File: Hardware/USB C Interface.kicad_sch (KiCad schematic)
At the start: 5 parts, among them J2 USB_C_Receptacle_USB2.0, U14 TPD4E02B04DQA

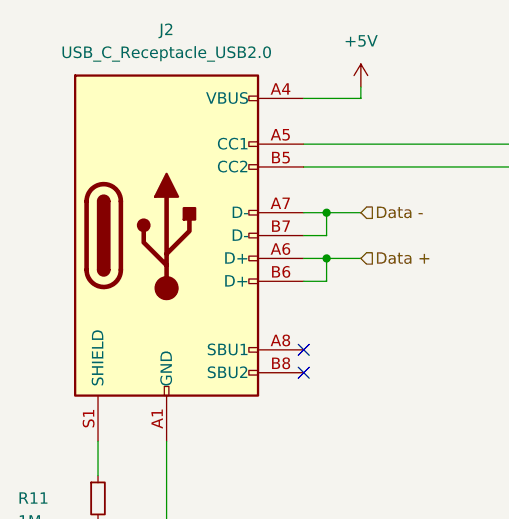
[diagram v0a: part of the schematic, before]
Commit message: Fix Reroute
Traces are getting messy, Moved the TOF sensors to be 3mm from edge of board. USB-C getting moved possibly. Changed Resistor and Capacitor footprints to better fit board space requirements.
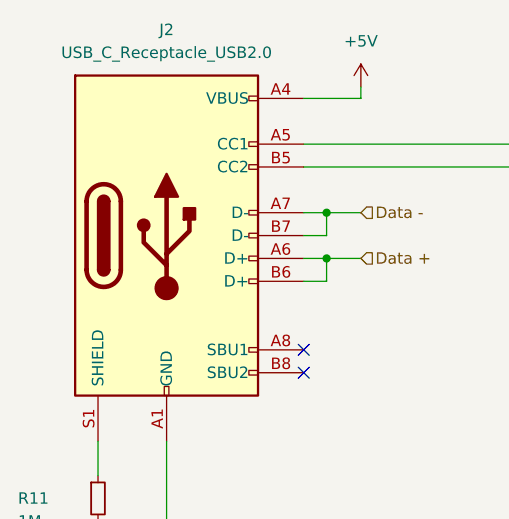
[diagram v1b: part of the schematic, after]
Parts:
- R11, R12, R13: footprint Resistor_SMD:R_0805_2012Metric -> Resistor_SMD:R_0402_1005Metric

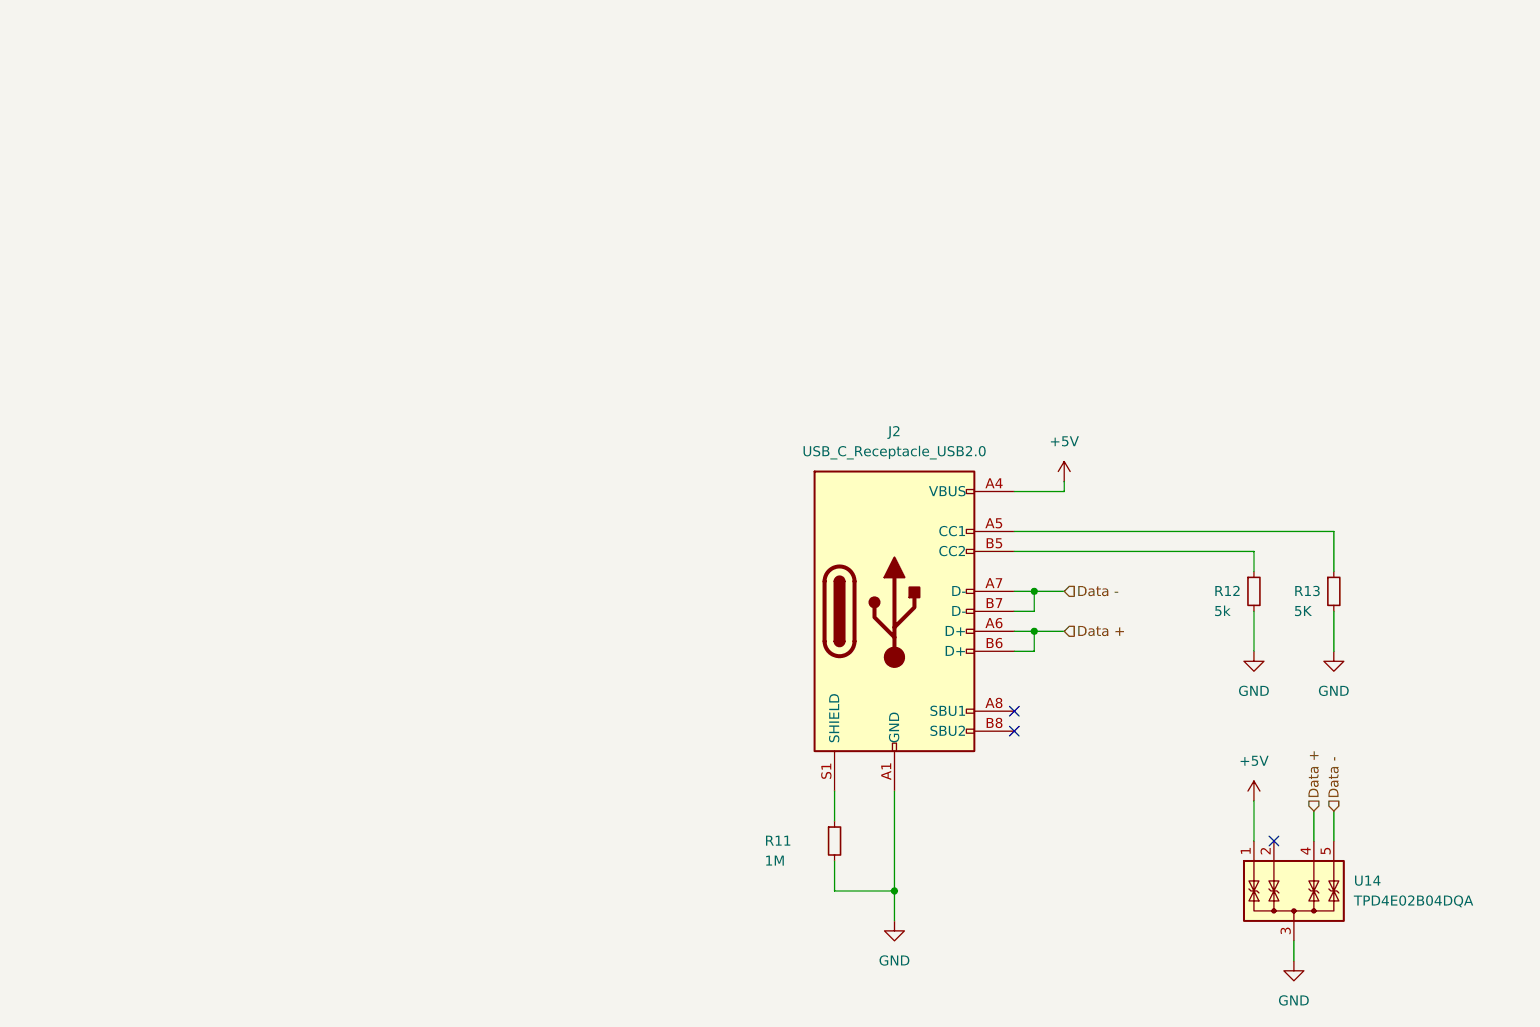
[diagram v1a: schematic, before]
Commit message: Squashed commit of the following:
commit e6d18f1838a18780ff985c290e2821e2ac438ddc
Author: KenwoodFox <kenwood364@gmail.com>
Date:   Sun Oct 5 18:23:23 2025 -0400

    Tweaked n' fixed things with @Amoskeag

commit 133f082a76a13551d058af83ac953c852f82cbfb
Author: Arthur Aznive <61330561+Amoskeag@users.noreply.github.com>
Date:   Sun Oct 5 10:51:39 2025 -0400

    Update I2C Bus Connections

    Channel 4 of I2C was not connected, will make traces pretty later.

commit 1fc084a3994e8cc2965589d6eb11268a7396225d
Author: Arthur Aznive <61330561+Amoskeag@users.noreply.github.com>
Date:   Sun Oct 5 10:36:15 2025 -0400

    Board Refactor, Updated Parts

    Updated Board layout and added new parts

commit 6f7fc722645cc0153b695158322b161c2f880b4a
Author: Arthur Aznive <61330561+Amoskeag@users.noreply.github.com>
Date:   Fri Oct 3 23:22:42 2025 -0400

    update 2025

    board refactor

commit 2a13c54343b839d82b0e646e49a68070081abc7a
Author: Arthur Aznive <61330561+Amoskeag@users.noreply.github.com>
Date:   Fri Oct 3 23:04:47 2025 -0400

    Square Board Time

    Rerouting, restarting project, trying to make a simpler dev board. Lets see what we can do.

commit d4ab96b311134bb0a7992d948496d7b671a058de
Author: Arthur Aznive <61330561+Amoskeag@users.noreply.github.com>
Date:   Wed Jan 15 14:01:24 2025 -0500

    4 L:ayer Board with USB-C

    Created a 4-Layer PCB with USB-C updates

commit 55621a658c07626f43cd5cc55c172a27abc51e41
Author: Arthur Aznive <61330561+Amoskeag@users.noreply.github.com>
Date:   Tue Mar 5 00:57:37 2024 -0500

    Updated Motor Driver Routing

    Working on Power Supply and Motor Controller Routing

commit 3f2874cc29094c27990d838de84f4fea139067e1
Author: Arthur Aznive <61330561+Amoskeag@users.noreply.github.com>
Date:   Sun Mar 3 23:13:56 2024 -0500

    BIG Changes

    Create a 4 Layer Variation
    Change Motor Controller routing.
    Change Power Regulation.
    Optimize Sensor routing.
    Pray I know what i'm doing

commit 08b48da4672d4d2e9f554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
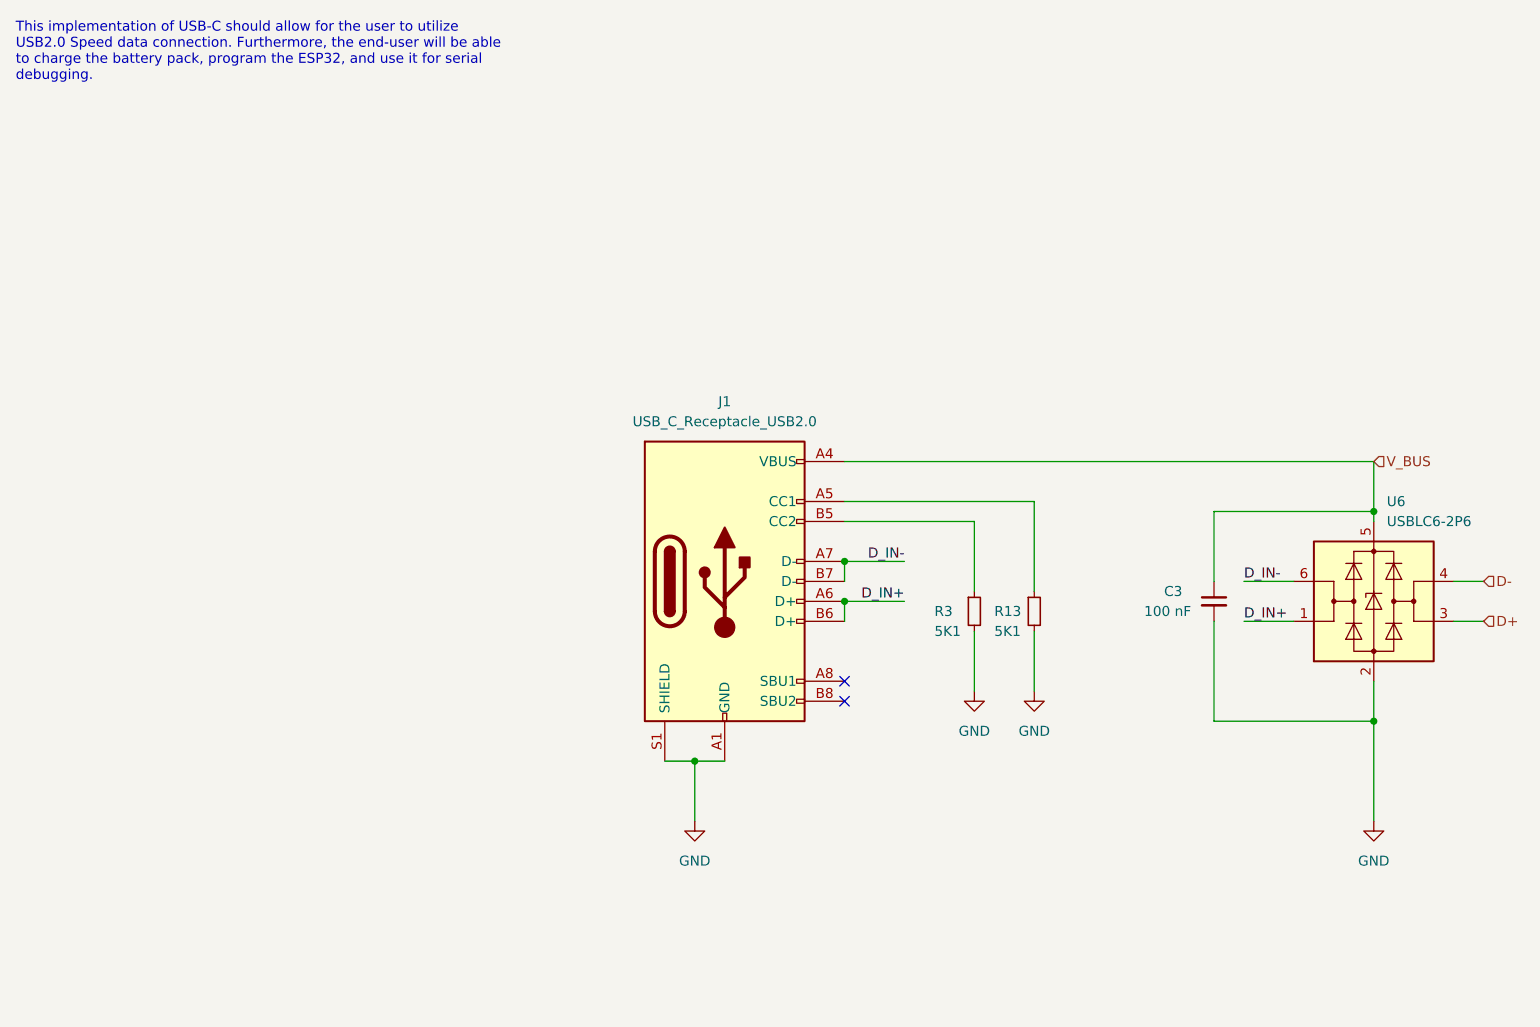
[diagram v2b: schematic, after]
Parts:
- removed J2: USB_C_Receptacle_USB2.0, Connector_USB:USB_C_Receptacle_XKB_U262-16XN-4BVC11, symbol Connector:USB_C_Receptacle_USB2.0
- removed R11: 1M, Resistor_SMD:R_0402_1005Metric, symbol Device:R_Small
- removed R12: 5k, Resistor_SMD:R_0402_1005Metric, symbol Device:R_Small
- removed U14: TPD4E02B04DQA, Package_SON:USON-10_2.5x1.0mm_P0.5mm, symbol Power_Protection:TPD4E02B04DQA
- added C3: 100 nF, Capacitor_SMD:C_0603_1608Metric, symbol Device:C_Small
- added J1: USB_C_Receptacle_USB2.0, Amoskeag_KiCAD_Lib:GCT_USB4110GFA, symbol Connector:USB_C_Receptacle_USB2.0
- added R3: 5K1, Resistor_SMD:R_0603_1608Metric, symbol Device:R_Small
- added U6: USBLC6-2P6, Package_TO_SOT_SMD:SOT-666, symbol Power_Protection:USBLC6-2P6
- R13: value 5K -> 5K1; footprint Resistor_SMD:R_0402_1005Metric -> Resistor_SMD:R_0603_1608Metric
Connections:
- net GND: now also C3.2, J1.A1 (GND), J1.A12 (GND), J1.B1 (GND), J1.B12 (GND), J1.S1 (SHIELD), R3.2, U6.2 (GND)
- net at R13.1: now also J1.A5 (CC1)
- new net: J1.B5 (CC2), R3.1
- new net D+: U6.3 (I/O2)
- new net D-: U6.4 (I/O2)
- new net D_IN+: J1.A6 (D+), J1.B6 (D+), U6.1 (I/O1)
- new net D_IN-: J1.A7 (D-), J1.B7 (D-), U6.6 (I/O1)
- new net V_BUS: C3.1, J1.A4 (VBUS), J1.A9 (VBUS), J1.B4 (VBUS), J1.B9 (VBUS), U6.5 (VBUS)
- no-connect marks 3 -> 2
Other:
- note added: "This implementation of USB-C should allow for the user to utilize USB2.0 Speed data connection. Furthermore, the end-user will be able to charge the battery pack, program the ESP32, and use it for serial debugging."
- moved on the sheet: R13
